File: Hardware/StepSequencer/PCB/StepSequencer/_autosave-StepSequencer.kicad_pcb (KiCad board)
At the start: 2 copper layers, 188 x 68.8 mm, 72 parts, among them J1 Conn_01x04_Male, U1 MCP23017_SP, U2 MCP23017_SP

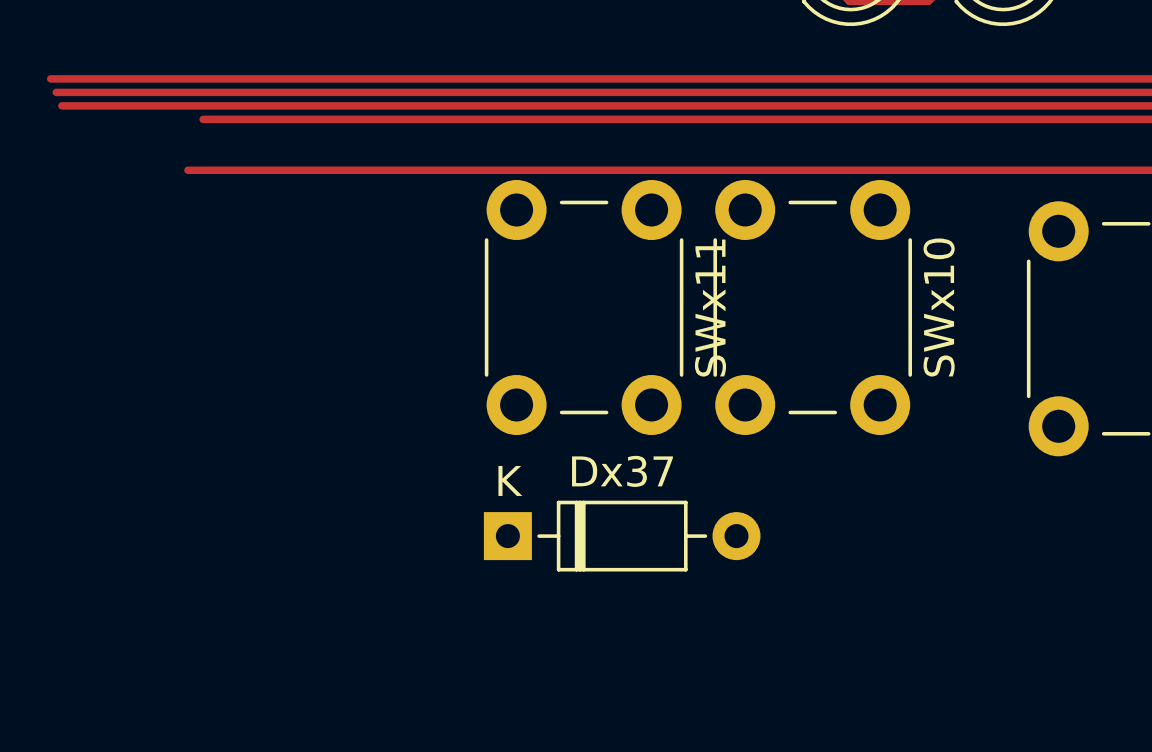
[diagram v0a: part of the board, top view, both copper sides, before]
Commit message: Recording multiple key press and tart of new hardware
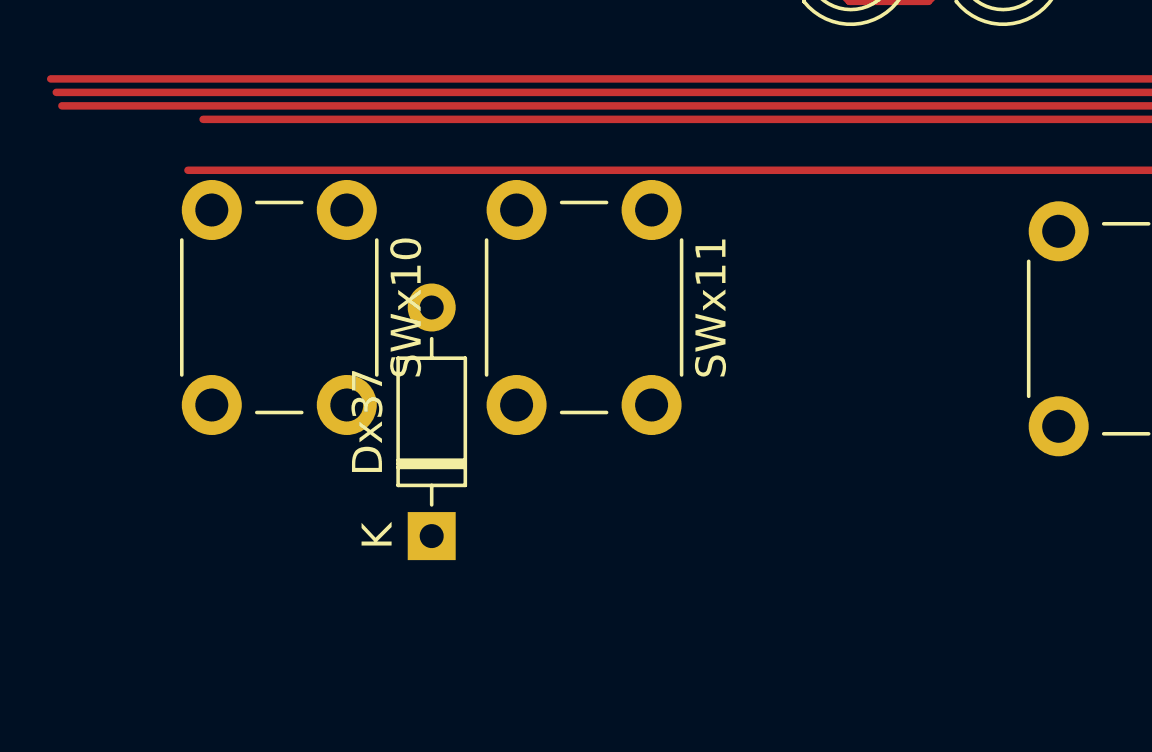
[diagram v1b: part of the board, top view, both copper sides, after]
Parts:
- moved SWx10 17.8 mm to (26.4, 65.4)
- moved Dx37 2.54 mm to (29.2, 76.2), turned to 90 degrees
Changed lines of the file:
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@@
   )
   (footprint "Button_Switch_THT:SW_PUSH_6mm" (layer "F.Cu")
-    (at 44.16 65.37 -90)
+    (at 26.38 65.37 -90)
     (descr "https://www.omron.com/ecb/products/pdf/en-b3f.pdf")
     (tags "tact sw push 6mm")
@@
   )
   (footprint "Diode_THT:D_DO-35_SOD27_P7.62mm_Horizontal" (layer "F.Cu")
-    (at 31.75 76.24)
+    (at 29.21 76.24 90)
     (descr "Diode, DO-35_SOD27 series, Axial, Horizontal, pin pitch=7.62mm, , length*diameter=4*2mm^2, , http://www.diodes.com/_files/packages/DO-35.pdf")
     (tags "Diode DO-35_SOD27 series Axial Horizontal pin pitch 7.62mm  length 4mm diameter 2mm")
@@
     (property "Sheetname" "")
     (attr through_hole)
-    (fp_text reference "Dx37" (at 3.81 -2.12) (layer "F.SilkS")
-      (effects (font (size 1 1) (thickness 0.15)))
-    )
-    (fp_text value "1N4148" (at 3.81 2.12) (layer "F.Fab")
-      (effects (font (size 1 1) (thickness 0.15)))
-    )
-    (fp_text user "K" (at 0 -1.8) (layer "F.SilkS")
-      (effects (font (size 1 1) (thickness 0.15)))
-    )
-    (fp_text user "K" (at 0 -1.8) (layer "F.Fab")
-      (effects (font (size 1 1) (thickness 0.15)))
-    )
-    (fp_text user "${REFERENCE}" (at 4.11 0) (layer "F.Fab")
+    (fp_text reference "Dx37" (at 3.81 -2.12 90) (layer "F.SilkS")
+      (effects (font (size 1 1) (thickness 0.15)))
+    )
+    (fp_text value "1N4148" (at 3.81 2.12 90) (layer "F.Fab")
+      (effects (font (size 1 1) (thickness 0.15)))
+    )
+    (fp_text user "K" (at 0 -1.8 90) (layer "F.SilkS")
+      (effects (font (size 1 1) (thickness 0.15)))
+    )
+    (fp_text user "K" (at 0 -1.8 90) (layer "F.Fab")
+      (effects (font (size 1 1) (thickness 0.15)))
+    )
+    (fp_text user "${REFERENCE}" (at 4.11 0 90) (layer "F.Fab")
       (effects (font (size 0.8 0.8) (thickness 0.12)))
     )
@@
     (fp_line (start 2.41 -1) (end 2.41 1) (layer "F.Fab") (width 0.1))
     (fp_line (start 7.62 0) (end 5.81 0) (layer "F.Fab") (width 0.1))
-    (pad "1" thru_hole rect (at 0 0) (size 1.6 1.6) (drill 0.8) (layers *.Cu *.Mask)
+    (pad "1" thru_hole rect (at 0 0 90) (size 1.6 1.6) (drill 0.8) (layers *.Cu *.Mask)
       (net 37 "GPD0") (pinfunction "K") (pintype "passive"))
-    (pad "2" thru_hole oval (at 7.62 0) (size 1.6 1.6) (drill 0.8) (layers *.Cu *.Mask)
+    (pad "2" thru_hole oval (at 7.62 0 90) (size 1.6 1.6) (drill 0.8) (layers *.Cu *.Mask)
       (net 60 "Net-(SWx1-Pad2)") (pinfunction "A") (pintype "passive"))
     (model "${KICAD6_3DMODEL_DIR}/Diode_THT.3dshapes/D_DO-35_SOD27_P7.62mm_Horizontal.wrl"
